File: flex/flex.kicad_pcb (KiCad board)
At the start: 2 copper layers, 126.3 x 113 mm, 105 parts, among them J1 Conn_01x06_Female, J2 Conn_01x05_Female, J3 Conn_01x03_Female, J4 Conn_01x06_Female, J5 Conn_01x03_Female, SW1 SW_Push, SW10 SW_Push, SW11 SW_Push, SW12 SW_Push, SW14 SW_Push, SW15 SW_Push, SW16 SW_Push, SW17 SW_Push, SW19 SW_Push, SW2 SW_Push, SW20 SW_Push, SW21 SW_Push, SW22 SW_Push, SW23 SW_Push, SW24 SW_Push, SW25 SW_Push, SW26 SW_Push, SW3 SW_Push, SW4 SW_Push, SW5 SW_Push, SW6 SW_Push, SW7 SW_Push, SW8 SW_Push, SW9 SW_Push

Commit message: edge cuts
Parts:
- removed D1, D10, D11, D12, D13, D14, D15, D16, D17, D31, D32, D9: D_Schottky_x2_KCom_AAK, customs:TSOT-23_HandSoldering
- added REF**: C_0201_0603Metric, Capacitor_SMD:C_0201_0603Metric, F.Cu at (53.4, 66.2)
- added REF**: C_0201_0603Metric, Capacitor_SMD:C_0201_0603Metric, F.Cu at (54.5, 68.0)
- added REF**: C_0201_0603Metric, Capacitor_SMD:C_0201_0603Metric, F.Cu at (54.5, 66.2)
- added REF**: C_0201_0603Metric, Capacitor_SMD:C_0201_0603Metric, F.Cu at (53.5, 69.9)
- added REF**: C_0201_0603Metric, Capacitor_SMD:C_0201_0603Metric, F.Cu at (54.8, 81.9)
- added REF**: C_0201_0603Metric, Capacitor_SMD:C_0201_0603Metric, F.Cu at (53.6, 80.0)
- added REF**: C_0201_0603Metric, Capacitor_SMD:C_0201_0603Metric, F.Cu at (53.7, 81.9)
- added REF**: C_0201_0603Metric, Capacitor_SMD:C_0201_0603Metric, F.Cu at (54.7, 80.0)
- added REF**: C_0201_0603Metric, Capacitor_SMD:C_0201_0603Metric, F.Cu at (54.5, 69.9)
- added REF**: C_0201_0603Metric, Capacitor_SMD:C_0201_0603Metric, F.Cu at (53.4, 68.0)
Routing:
- net (no net): track 0.00 -> 1.80 mm
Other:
- outline, holes or cut-outs redrawn

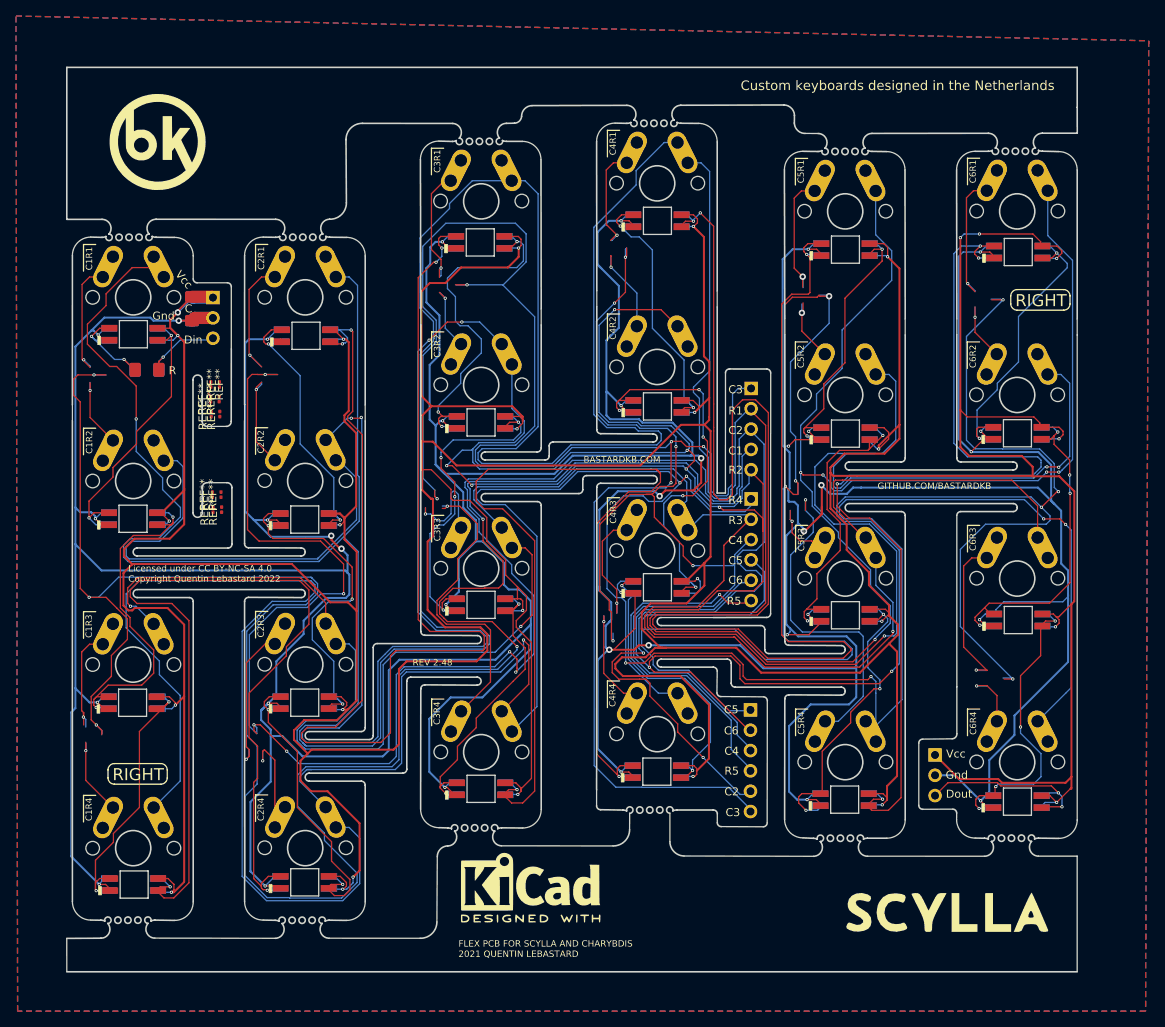
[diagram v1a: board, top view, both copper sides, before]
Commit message: update diodes and leds
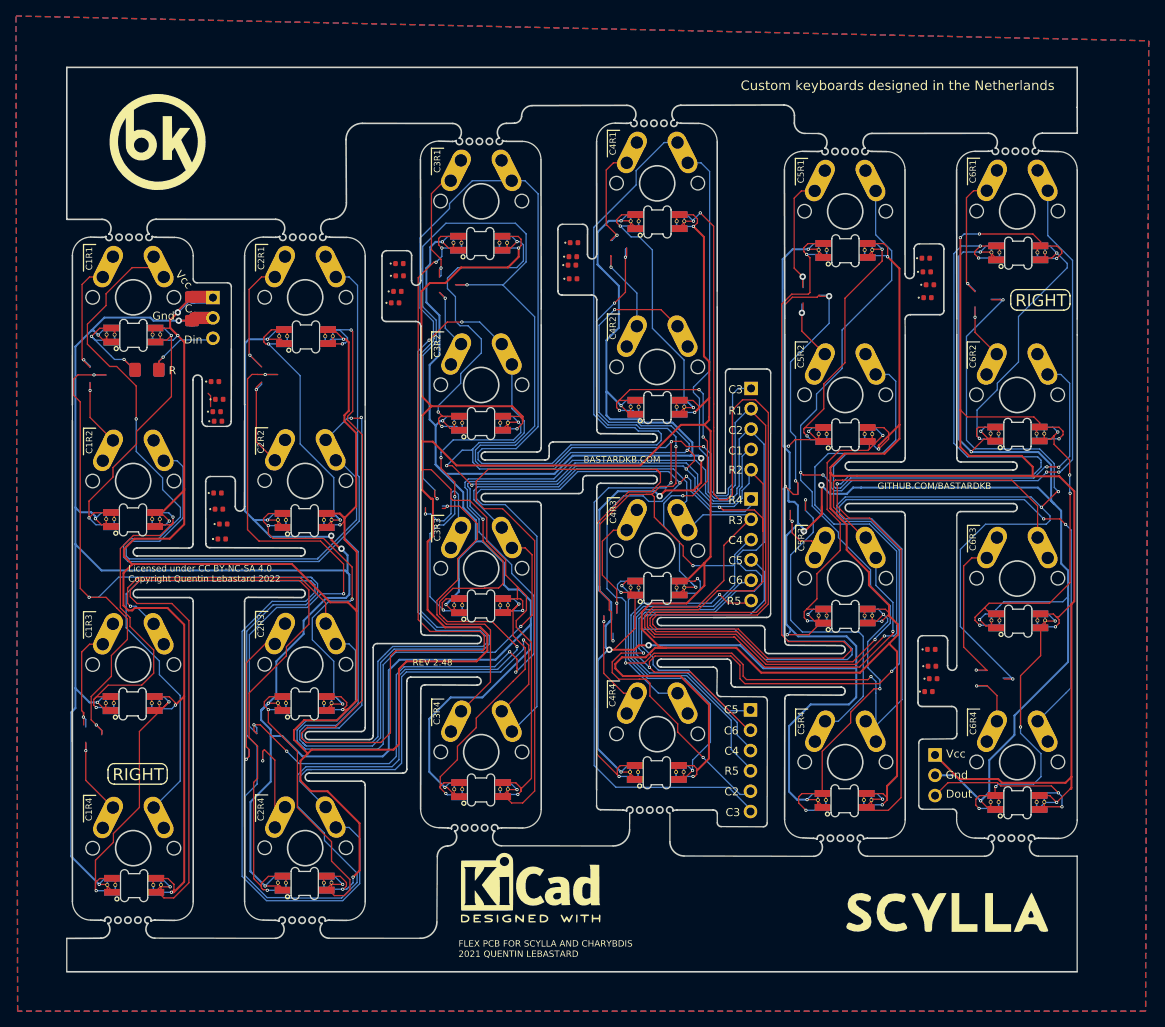
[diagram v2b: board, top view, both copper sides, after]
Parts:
- removed the D20 at (87.1, 48.5)
- removed the D22 at (87.2, 71.0)
- removed the D24 at (87.2, 93.8)
- removed the D38 at (109.2, 114.6)
- removed the D40 at (109.3, 91.6)
- removed the D42 at (109.3, 69.0)
- removed the D44 at (109.3, 45.8)
- removed the D46 at (132.8, 49.4)
- removed the D48 at (132.8, 72.4)
- removed D50, D52, D54, D56, D58, D60: SK6812MINI, libs2:YS-SK6812MINI-E_REVERSE_NO_EDGECUT
- removed the G*** at (366.7, 111.2)
- removed the G*** at (277.7, 122.3)
- removed the G*** at (278.1, 122.6)
- removed the G*** at (366.4, 111.2)
- removed the G*** at (266.9, 142.5)
- removed the G*** at (267.0, 148.6)
- removed REF** (x10): C_0201_0603Metric, Capacitor_SMD:C_0201_0603Metric
- added D1: 1N4148, libs:D_0402, F.Cu at (54.3, 79.8)
- added D10: 1N4148, libs:D_0402, F.Cu at (143.3, 53.8)
- added D11: 1N4148, libs:D_0402, F.Cu at (76.8, 54.6)
- added D12: 1N4148, libs:D_0402, F.Cu at (143.6, 101.4)
- added D2: 1N4148, libs:D_0402, F.Cu at (98.7, 53.0)
- added D25: 1N4148, libs:D_0402, F.Cu at (53.9, 65.9)
- added D3: 1N4148, libs:D_0402, F.Cu at (54.4, 81.8)
- added D31: 1N4148, libs:D_0402, F.Cu at (54.3, 70.8)
- added D32: 1N4148, libs:D_0402, F.Cu at (76.5, 56.0)
- added D33: 1N4148, libs:D_0402, F.Cu at (55.0, 83.7)
- added D35: 1N4148, libs:D_0402, F.Cu at (143.0, 55.4)
- added D4: 1N4148, libs:D_0402, F.Cu at (77.0, 51.1)
- added D5: 1N4148, libs:D_0402, F.Cu at (142.8, 50.4)
- added D7: 1N4148, libs:D_0402, F.Cu at (98.7, 50.2)
- added D9: 1N4148, libs:D_0402, F.Cu at (98.8, 48.5)
- D13: renamed from D2; footprint libs2:YS-SK6812MINI-E_REVERSE -> libs:SK6812_mini_e_corners
- D14: renamed from D3; footprint libs2:YS-SK6812MINI-E_REVERSE -> libs:SK6812_mini_e_corners
- D15: renamed from D4; footprint libs2:YS-SK6812MINI-E_REVERSE -> libs:SK6812_mini_e_corners
- D16: renamed from D18; footprint libs2:YS-SK6812MINI-E_REVERSE -> libs:SK6812_mini_e_corners
- D17: renamed from D5; footprint libs2:YS-SK6812MINI-E_REVERSE -> libs:SK6812_mini_e_corners
- D18: renamed from D7; footprint libs2:YS-SK6812MINI-E_REVERSE -> libs:SK6812_mini_e_corners
- D19: renamed from D33; footprint libs2:YS-SK6812MINI-E_REVERSE -> libs:SK6812_mini_e_corners
- D20: renamed from D35; footprint libs2:YS-SK6812MINI-E_REVERSE -> libs:SK6812_mini_e_corners
- D21: renamed from D19; footprint libs2:YS-SK6812MINI-E_REVERSE -> libs:SK6812_mini_e_corners
- D22: renamed from D21; footprint libs2:YS-SK6812MINI-E_REVERSE -> libs:SK6812_mini_e_corners
- D23, D37: footprint libs2:YS-SK6812MINI-E_REVERSE -> libs:SK6812_mini_e_corners
- D24: renamed from D25; footprint libs2:YS-SK6812MINI-E_REVERSE -> libs:SK6812_mini_e_corners
- D26, D27, D28, D29, D30, D34, D36, D6, D8: value SK6812MINI -> 1N4148; footprint libs2:YS-SK6812MINI-E_REVERSE_NO_EDGECUT -> libs:D_0402; moved to F.Cu
- D38: renamed from D39; footprint libs2:YS-SK6812MINI-E_REVERSE -> libs:SK6812_mini_e_corners
- D39: renamed from D41; footprint libs2:YS-SK6812MINI-E_REVERSE -> libs:SK6812_mini_e_corners
- D40: renamed from D43; footprint libs2:YS-SK6812MINI-E_REVERSE -> libs:SK6812_mini_e_corners
- D41: renamed from D45; footprint libs2:YS-SK6812MINI-E_REVERSE -> libs:SK6812_mini_e_corners
- D42: renamed from D47; footprint libs2:YS-SK6812MINI-E_REVERSE -> libs:SK6812_mini_e_corners
- D43: renamed from D49; footprint libs2:YS-SK6812MINI-E_REVERSE -> libs:SK6812_mini_e_corners
- D44: renamed from D51; footprint libs2:YS-SK6812MINI-E_REVERSE -> libs:SK6812_mini_e_corners
- D45: renamed from D53; footprint libs2:YS-SK6812MINI-E_REVERSE -> libs:SK6812_mini_e_corners
- D46: renamed from D55; footprint libs2:YS-SK6812MINI-E_REVERSE -> libs:SK6812_mini_e_corners
- D47: renamed from D57; footprint libs2:YS-SK6812MINI-E_REVERSE -> libs:SK6812_mini_e_corners
- D48: renamed from D59; footprint libs2:YS-SK6812MINI-E_REVERSE -> libs:SK6812_mini_e_corners
- moved D6 108.9 mm to (142.9, 52.1)
- moved D30 103.2 mm to (143.7, 103.0)
- moved D29 99.4 mm to (143.1, 104.6)
- moved D36 87.4 mm to (143.5, 99.3)
- moved D28 63.3 mm to (98.6, 51.3)
- moved D26 58.7 mm to (54.5, 68.1)
- moved D8 38.0 mm to (54.2, 69.6)
- moved D27 34.1 mm to (77.0, 52.6)
- moved D34 10.7 mm to (54.8, 85.5)
- renumbered J4 to J3, J3 to J4, SW9 to SW1, SW15 to SW10, SW20 to SW11, SW24 to SW12, SW3 to SW13, SW7 to SW14, SW11 to SW15, SW21 to SW17, SW25 to SW18, SW4 to SW19, SW14 to SW2, SW8 to SW20, SW12 to SW21, SW17 to SW22, SW22 to SW23, SW26 to SW24, SW19 to SW3, SW23 to SW4, SW1 to SW5, SW5 to SW6, SW2 to SW7, SW6 to SW8, SW10 to SW9
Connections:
- D13 pad 1: Net-(D2-Pad1) -> Net-(D13-DOUT)
- D13 pad 3: Net-(D2-Pad3) -> Net-(D13-DIN)
- D14 pad 1: Net-(D28-Pad1) -> Net-(D14-DOUT)
- D14 pad 3: Net-(D2-Pad1) -> Net-(D13-DOUT)
- D15 pad 1: Net-(D18-Pad3) -> Net-(D15-DOUT)
- D15 pad 3: Net-(D28-Pad1) -> Net-(D14-DOUT)
- D16 pad 1: Net-(D18-Pad1) -> Net-(D16-DOUT)
- D16 pad 3: Net-(D18-Pad3) -> Net-(D15-DOUT)
- D17 pad 1: Net-(D5-Pad1) -> Net-(D17-DOUT)
- D17 pad 3: Net-(D18-Pad1) -> Net-(D16-DOUT)
- D18 pad 1: Net-(D33-Pad3) -> Net-(D18-DOUT)
- D18 pad 3: Net-(D5-Pad1) -> Net-(D17-DOUT)
- D19 pad 1: Net-(D33-Pad1) -> Net-(D19-DOUT)
- D19 pad 3: Net-(D33-Pad3) -> Net-(D18-DOUT)
- D20 pad 1: Net-(D19-Pad3) -> Net-(D20-DOUT)
- D20 pad 3: Net-(D33-Pad1) -> Net-(D19-DOUT)
- D21 pad 3: Net-(D19-Pad3) -> Net-(D20-DOUT)
- D23 pad 1: Net-(D23-Pad1) -> Net-(D23-DOUT)
- D24 pad 1: Net-(D25-Pad1) -> Net-(D24-DOUT)
- D24 pad 3: Net-(D23-Pad1) -> Net-(D23-DOUT)
- D26 pad 1: Net-(D25-Pad1) -> col1
- D26 pad 2: Gnd -> Net-(D26-A)
- D27 pad 1: Net-(D2-Pad1) -> col3
- D27 pad 2: Gnd -> Net-(D27-A)
- D28 pad 1: Net-(D28-Pad1) -> col4
- D28 pad 2: Gnd -> Net-(D28-A)
- D29 pad 1: Net-(D18-Pad3) -> col6
- D29 pad 2: Gnd -> Net-(D29-A)
- D30 pad 1: Net-(D18-Pad1) -> col6
- D30 pad 2: Gnd -> Net-(D30-A)
- D34 pad 1: Net-(D33-Pad1) -> col2
- D34 pad 2: Gnd -> Net-(D34-A)
- D36 pad 1: Net-(D19-Pad3) -> col6
- D36 pad 2: Gnd -> Net-(D36-A)
- D37 pad 3: Net-(D25-Pad1) -> Net-(D24-DOUT)
- D6 pad 1: Net-(D5-Pad1) -> col5
- D6 pad 2: Gnd -> Net-(D6-A)
- D8 pad 1: Net-(D33-Pad3) -> col1
- D8 pad 2: Gnd -> Net-(D8-A)
- R1 pad 2: Net-(D2-Pad3) -> Net-(D13-DIN)
- R2 pad 2: Net-(D2-Pad3) -> Net-(D13-DIN)
- SW10 pad 2: Net-(D11-Pad1) -> Net-(D28-A)
- SW11 pad 2: Net-(D14-Pad1) -> Net-(D6-A)
- SW12 pad 2: Net-(D16-Pad1) -> Net-(D30-A)
- SW13 pad 2: Net-(D1-Pad2) -> Net-(D8-A)
- SW20 pad 2: Net-(D32-Pad1) -> Net-(D34-A)
- SW24 pad 2: Net-(D17-Pad1) -> Net-(D36-A)
- SW4 pad 2: Net-(D16-Pad2) -> Net-(D29-A)
- SW7 pad 2: Net-(D13-Pad1) -> Net-(D26-A)
- SW9 pad 2: Net-(D9-Pad1) -> Net-(D27-A)
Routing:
- net Net-(D20-DOUT): track 0.00 -> 164.0 mm, vias 0 -> 4
- net Net-(D19-Pad3): track 164.0 -> 0.00 mm, vias 4 -> 0
- net Net-(D25-Pad1): track 125.7 -> 0.00 mm, vias 2 -> 0
- net Net-(D24-DOUT): track 0.00 -> 125.7 mm, vias 0 -> 2
- net Net-(D18-Pad1): track 122.0 -> 0.00 mm, vias 2 -> 0
- net Net-(D16-DOUT): track 0.00 -> 122.0 mm, vias 0 -> 2
- net Net-(D33-Pad3): track 45.6 -> 0.00 mm, vias 3 -> 0
- net Net-(D18-DOUT): track 0.00 -> 45.6 mm, vias 0 -> 3
- net Net-(D28-Pad1): track 44.5 -> 0.00 mm, vias 2 -> 0
- net Net-(D14-DOUT): track 0.00 -> 44.5 mm, vias 0 -> 2
- net Net-(D5-Pad1): track 40.1 -> 0.00 mm, vias 2 -> 0
- net Net-(D17-DOUT): track 0.00 -> 40.1 mm, vias 0 -> 2
- net Net-(D23-Pad1): track 38.2 -> 0.00 mm, vias 2 -> 0
- net Net-(D23-DOUT): track 0.00 -> 38.2 mm, vias 0 -> 2
- net Net-(D2-Pad1): track 37.7 -> 0.00 mm, vias 2 -> 0
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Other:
- outline, holes or cut-outs redrawn

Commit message: emergency diodes
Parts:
- added D49: 1N4148, custom:Diode_TH_SOD123, F.Cu at (37.8, 64.9)
- added D50: 1N4148, custom:Diode_TH_SOD123, F.Cu at (37.8, 87.8)
- added D51: 1N4148, custom:Diode_TH_SOD123, F.Cu at (37.8, 110.8)
- added D52: 1N4148, custom:Diode_TH_SOD123, F.Cu at (37.8, 133.8)
- added D53: 1N4148, custom:Diode_TH_SOD123, F.Cu at (71.2, 65.3)
- added D54: 1N4148, custom:Diode_TH_SOD123, F.Cu at (71.2, 88.2)
- added D55: 1N4148, custom:Diode_TH_SOD123, F.Cu at (71.2, 111.0)
- added D56: 1N4148, custom:Diode_TH_SOD123, F.Cu at (71.2, 133.8)
- added D57: 1N4148, custom:Diode_TH_SOD123, F.Cu at (93.2, 53.5)
- added D58: 1N4148, custom:Diode_TH_SOD123, F.Cu at (93.2, 76.3)
- added D59: 1N4148, custom:Diode_TH_SOD123, F.Cu at (93.2, 99.1)
- added D60: 1N4148, custom:Diode_TH_SOD123, F.Cu at (93.2, 121.9)
- added D61: 1N4148, custom:Diode_TH_SOD123, F.Cu at (103.3, 50.8)
- added D62: 1N4148, custom:Diode_TH_SOD123, F.Cu at (103.3, 73.7)
- added D63: 1N4148, custom:Diode_TH_SOD123, F.Cu at (103.3, 96.6)
- added D64: 1N4148, custom:Diode_TH_SOD123, F.Cu at (103.3, 119.4)
- added D65: 1N4148, custom:Diode_TH_SOD123, F.Cu at (126.9, 54.2)
- added D66: 1N4148, custom:Diode_TH_SOD123, F.Cu at (126.9, 77.2)
- added D67: 1N4148, custom:Diode_TH_SOD123, F.Cu at (126.9, 100.1)
- added D68: 1N4148, custom:Diode_TH_SOD123, F.Cu at (126.9, 123.1)
- added D69: 1N4148, custom:Diode_TH_SOD123, F.Cu at (148.7, 53.9)
- added D70: 1N4148, custom:Diode_TH_SOD123, F.Cu at (148.7, 77.1)
- added D71: 1N4148, custom:Diode_TH_SOD123, F.Cu at (148.7, 100.3)
- added D72: 1N4148, custom:Diode_TH_SOD123, F.Cu at (148.7, 123.5)
- moved D34 4.20 mm to (54.6, 81.3)
- moved D29 3.52 mm to (143.6, 101.1)
- moved D33 3.42 mm to (54.6, 80.3)
- moved D2 3.29 mm to (98.6, 49.7)
- moved D35 3.10 mm to (143.1, 52.3)
- moved D32 2.95 mm to (76.7, 53.1)
- moved D30 2.91 mm to (143.6, 100.1)
- moved D3 2.64 mm to (54.6, 79.2)
- moved D7 2.63 mm to (98.6, 47.6)
- moved D28 2.63 mm to (98.6, 48.7)
- moved D10 2.57 mm to (143.1, 51.2)
- moved D11 2.57 mm to (76.7, 52.0)
- moved D12 2.38 mm to (143.6, 99.1)
- moved D6 2.03 mm to (143.1, 50.1)
- moved D9 1.94 mm to (98.6, 46.6)
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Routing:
- net col1: track 286.0 -> 287.9 mm
- net (no net): track 1.80 -> 0.00 mm
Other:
- outline, holes or cut-outs redrawn

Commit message: routing
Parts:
- removed C1, C2: C, Capacitor_SMD:C_1206_3216Metric_Pad1.42x1.75mm_HandSolder
- removed R1, R2: R, Resistor_SMD:R_1206_3216Metric_Pad1.42x1.75mm_HandSolder
- moved D54 18.3 mm to (70.0, 69.9), turned to 180 degrees
- moved D53 11.6 mm to (59.6, 65.0)
- moved D55 11.6 mm to (59.6, 110.7)
- moved D56 11.6 mm to (59.6, 133.5)
- moved D57 11.6 mm to (81.6, 53.1)
- moved D58 11.6 mm to (81.6, 75.9)
- moved D59 11.6 mm to (81.6, 98.7)
- moved D60 11.6 mm to (81.6, 121.5)
- moved D2 3.18 mm to (98.2, 46.6)
- moved D9 3.18 mm to (98.2, 49.7)
- moved D36 3.17 mm to (143.3, 101.2)
- moved D29 3.07 mm to (143.3, 98.1)
- moved D12 1.14 mm to (143.3, 100.1)
- moved D28 1.13 mm to (98.2, 47.6)
- moved D7 1.13 mm to (98.2, 48.7)
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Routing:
- net Vcc: track 926.6 -> 0.00 mm, vias 28 -> 0
- net Gnd: track 897.9 -> 0.00 mm, vias 36 -> 0
- net row1: track 655.7 -> 424.1 mm, vias 6 -> 5
- net row2: track 513.7 -> 282.7 mm, vias 13 -> 4
- net col6: track 204.1 -> 3.10 mm, vias 6 -> 0
- net Net-(D40-DOUT): track 192.7 -> 0.00 mm, vias 3 -> 0
- net Net-(D20-DOUT): track 164.0 -> 0.00 mm, vias 4 -> 0
- net col5: track 160.7 -> 3.23 mm, vias 3 -> 0
- net row4: track 431.2 -> 280.0 mm, vias 7 -> 4
- net col1: track 287.9 -> 154.6 mm, vias 5 -> 1
- net Net-(D44-DOUT): track 126.2 -> 0.00 mm, vias 4 -> 0
- net Net-(D24-DOUT): track 125.7 -> 0.00 mm, vias 2 -> 0
- net Net-(D16-DOUT): track 122.0 -> 0.00 mm, vias 2 -> 0
- net Net-(D31-A): track 10.6 -> 94.6 mm, vias 1 -> 0
- net Net-(D64-A): track 13.1 -> 88.5 mm, vias 1 -> 0
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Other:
- copper layers 2 -> 4
